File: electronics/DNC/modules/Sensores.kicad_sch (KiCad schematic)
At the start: 10 parts

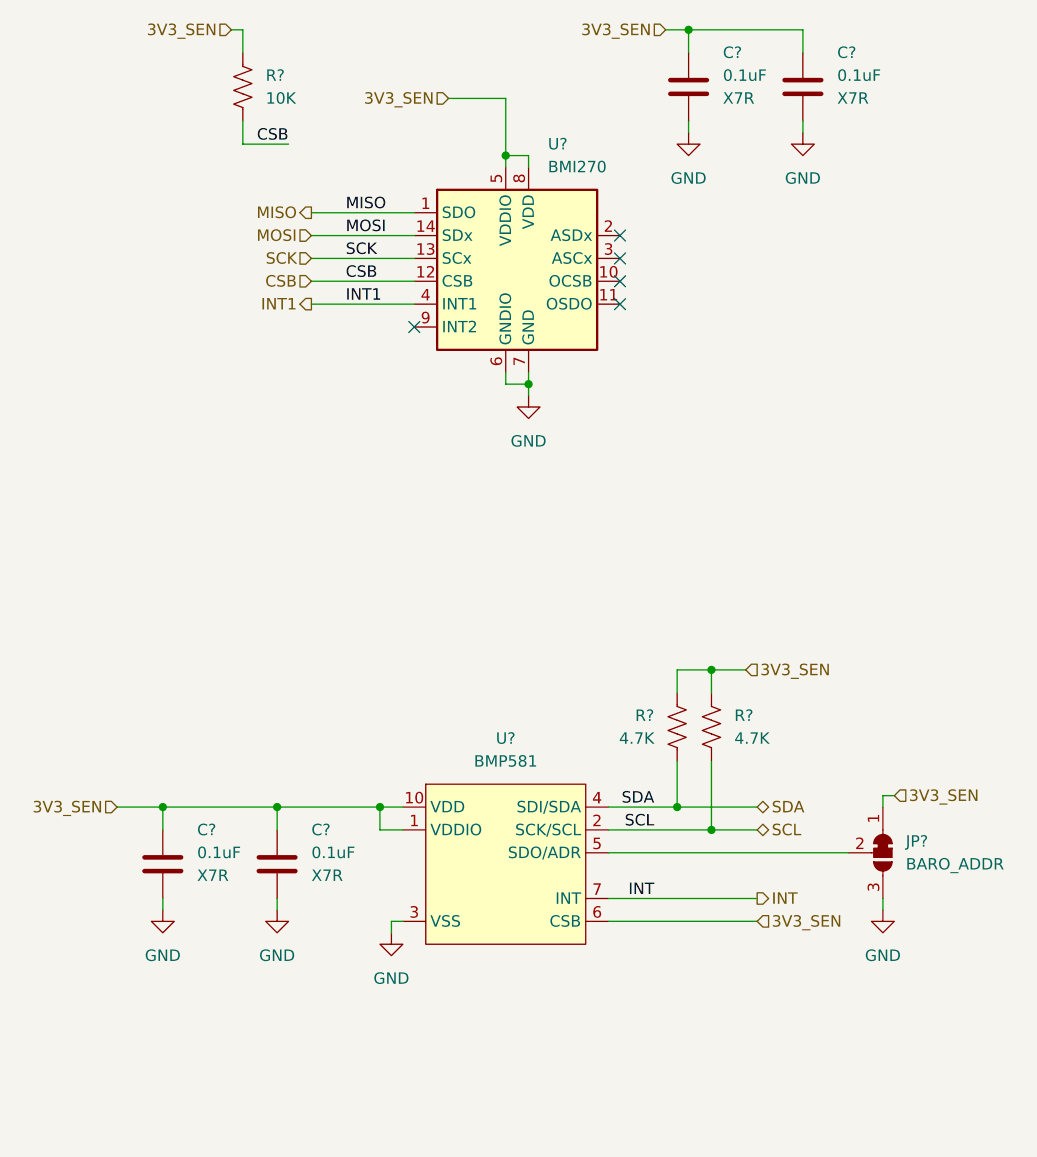
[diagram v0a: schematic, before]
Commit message: Se enlazó el BMP581 a SJ_Sensor y la hoja de dibujo a sj_library
- Sensores: BMP581 pasa de MSS_Sensor (librería de MS4M) a SJ_Sensor:BMP581 con la
  huella Bosch_LGA-10_2x2mm_P0.5mm (antes usaba la huella del LPS22). Reruteado;
  netlist verificado: mismas redes, y VSS 8/9 ahora conectados explícitamente a GND.
- DNC.kicad_pro: hoja de dibujo desde ${SJ_KICAD_LIBS}/sj_library/worksheets/SJ_Page.kicad_wks
  (antes ${MS4M_TEMPLATE}).
- El proyecto ya no depende de ninguna librería de MS4M.

Co-Authored-By: Claude Opus 5.5 <noreply@anthropic.com>
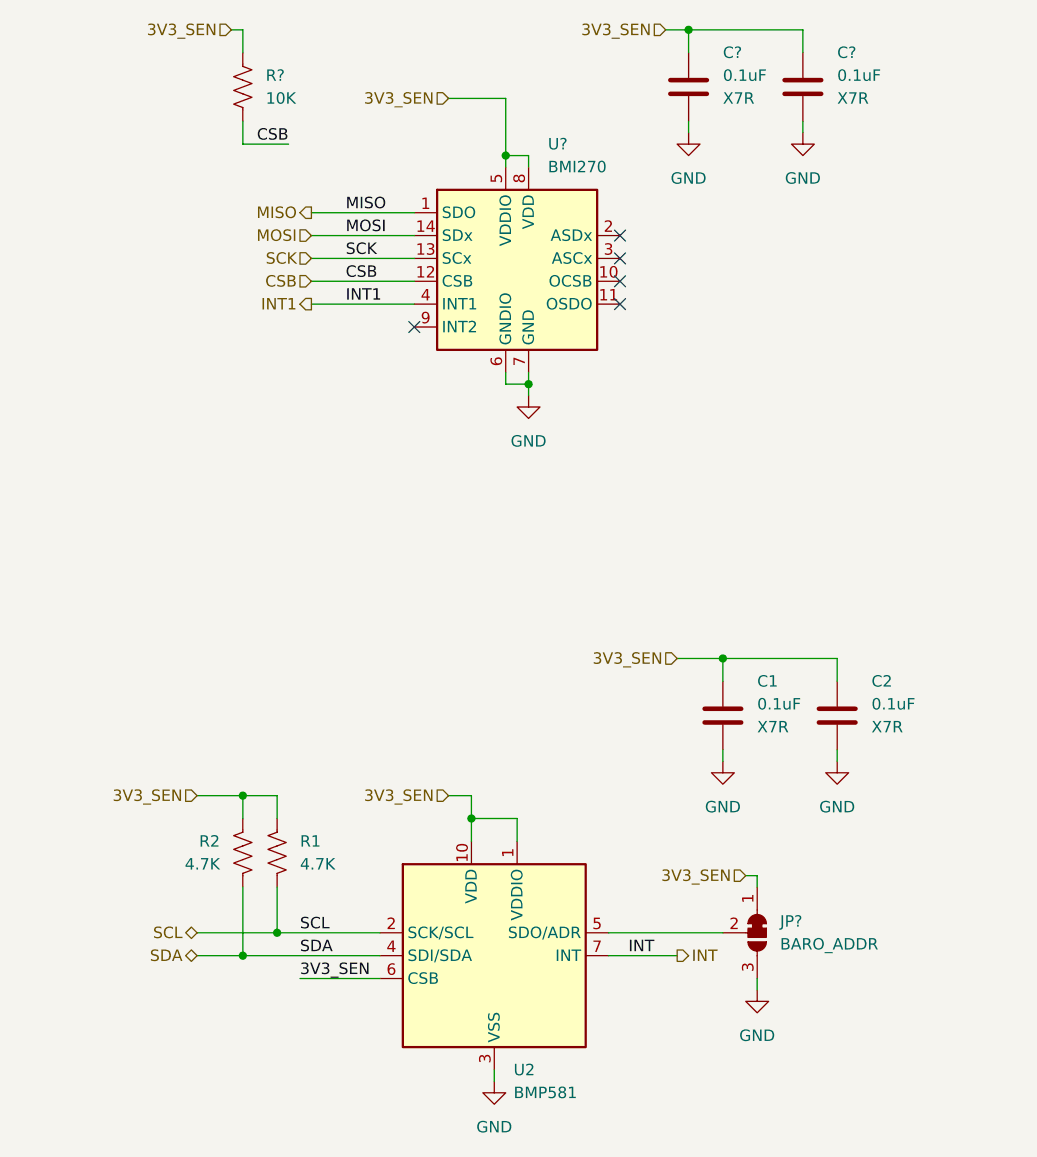
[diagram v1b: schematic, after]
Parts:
- removed C? (x2): 0.1uF, symbol Device:C
- removed R? (x2): 4.7K, symbol Device:R_US
- removed U?: BMP581, Package_LGA:ST_HLGA-10_2x2mm_P0.5mm_LayoutBorder3x2y, symbol MSS_Sensor:BMP581
- added C1, C2: 0.1uF, symbol Device:C
- added R1, R2: 4.7K, symbol Device:R_US
- added U2: BMP581, SJ_Sensor:Bosch_LGA-10_2x2mm_P0.5mm, symbol SJ_Sensor:BMP581
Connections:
- net 3V3_SEN: now also C1.1, C2.1, R1.1, R2.1, U2.1 (VDDIO), U2.10 (VDD), U2.6 (CSB)
- net GND: now also C1.2, C2.2, U2.3 (VSS), U2.8 (VSS), U2.9 (VSS)
- net INT: now also U2.7 (INT)
- net SCL: now also R1.2, U2.2 (SCK/SCL)
- net SDA: now also R2.2, U2.4 (SDI/SDA)
- net at JP?.2 (C): now also U2.5 (SDO/ADR)
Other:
- moved on the sheet: JP?

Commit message: XT60 con huella estándar y BMI270 enlazado a SJ_Sensor
- XT60: Gen_devices:AMASS_XT60-M -> Connector_AMASS:AMASS_XT60-M_1x02_P7.20mm_Vertical
  (misma geometría y polaridad: pin 1 GND, pin 2 VIN_RAW), con los campos SJ.
- Sensores: BMI270 pasa de Sensor_Motion:BMI160 a SJ_Sensor:BMI270 (misma geometría;
  netlist idéntico, sin cambios de cableado). Pines sin usar según Bosch: ASDx/ASCx,
  INT2, OCSB y OSDO sin conectar.

Co-Authored-By: Claude Opus 5.5 <noreply@anthropic.com>
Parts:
- removed U?: BMI270, Package_LGA:Bosch_LGA-14_3x2.5mm_P0.5mm, symbol Sensor_Motion:BMI160
- added U?: BMI270, Package_LGA:Bosch_LGA-14_3x2.5mm_P0.5mm, symbol SJ_Sensor:BMI270
- renumbered C1 to C?, C2 to C?, R2 to R?, R1 to R?, U2 to U?
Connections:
- net 3V3_SEN: now also U?.5 (VDDIO), U?.8 (VDD)
- net CSB: now also U?.12 (CSB)
- net GND: now also U?.6 (GNDIO), U?.7 (GND)
- net INT1: now also U?.4 (INT1)
- net MISO: now also U?.1 (SDO)
- net MOSI: now also U?.14 (SDx)
- net SCK: now also U?.13 (SCx)
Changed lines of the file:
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@@
 	)
 	(symbol
-		(lib_id "Sensor_Motion:BMI160")
+		(lib_id "SJ_Sensor:BMI270")
 		(at 82.55 76.2 0)
 		(unit 1)
@@
 			)
 		)
-		(property "Description" "Accelerometer, Gyroscope, 6 Axis Sensor I2C, SPI Output"
+		(property "Description" "6-axis IMU (accelerometer + gyroscope), SPI/I2C, OIS/AUX interface, 1.71-3.6V, LGA-14 3x2.5mm"
 			(at 82.55 76.2 0)
 			(hide yes)
@@
 		(property "Voltage" ""
 			(at 82.55 76.2 0)
+			(hide yes)
 			(show_name no)
 			(do_not_autoplace no)
@@
 		(property "Current" ""
 			(at 82.55 76.2 0)
+			(hide yes)
 			(show_name no)
 			(do_not_autoplace no)
@@
 		(property "TC" ""
 			(at 82.55 76.2 0)
+			(hide yes)
 			(show_name no)
 			(do_not_autoplace no)
@@
 		(property "Power" ""
 			(at 82.55 76.2 0)
+			(hide yes)
 			(show_name no)
 			(do_not_autoplace no)
@@
 		(property "Tol" ""
 			(at 82.55 76.2 0)
-			(show_name no)
-			(do_not_autoplace no)
-			(effects
-				(font
-					(size 1.27 1.27)
-				)
-			)
+			(hide yes)
+			(show_name no)
+			(do_not_autoplace no)
+			(effects
+				(font
+					(size 1.27 1.27)
+				)
+			)
+		)
+		(pin "5"
+		)
+		(pin "12"
 		)
 		(pin "4"
 		)
+		(pin "3"
+		)
+		(pin "1"
+		)
+		(pin "7"
+		)
+		(pin "6"
+		)
+		(pin "9"
+		)
 		(pin "11"
 		)
-		(pin "5"
-		)
-		(pin "6"
-		)
-		(pin "1"
+		(pin "2"
+		)
+		(pin "8"
 		)
 		(pin "10"
 		)
-		(pin "8"
-		)
-		(pin "2"
-		)
-		(pin "12"
-		)
-		(pin "3"
-		)
 		(pin "13"
 		)
-		(pin "9"
-		)
 		(pin "14"
-		)
-		(pin "7"
 		)
 		(instances
@@
 		(dnp no)
 		(fields_autoplaced yes)
-		(property "Reference" "R2"
+		(property "Reference" "R?"
 			(at 48.26 140.9699 0)
 			(show_name no)
@@
 			(project "DNC"
 				(path "/abee636e-ad3a-4ba4-b95f-d0cf4a6d3d85/c7e61742-03fb-4f4f-aef3-37e8cfb255c2"
-					(reference "R2")
+					(reference "R?")
 					(unit 1)
 				)
@@
 		(dnp no)
 		(fields_autoplaced yes)
-		(property "Reference" "C1"
+		(property "Reference" "C?"
 			(at 107.95 123.1899 0)
 			(show_name no)
@@
 			(project "DNC"
 				(path "/abee636e-ad3a-4ba4-b95f-d0cf4a6d3d85/c7e61742-03fb-4f4f-aef3-37e8cfb255c2"
-					(reference "C1")
+					(reference "C?")
 					(unit 1)
 				)
@@
 		(dnp no)
 		(fields_autoplaced yes)
-		(property "Reference" "R1"
+		(property "Reference" "R?"
 			(at 57.15 140.9699 0)
 			(show_name no)
@@
 			(project "DNC"
 				(path "/abee636e-ad3a-4ba4-b95f-d0cf4a6d3d85/c7e61742-03fb-4f4f-aef3-37e8cfb255c2"
-					(reference "R1")
+					(reference "R?")
 					(unit 1)
 				)
@@
 		(dnp no)
 		(fields_autoplaced yes)
-		(property "Reference" "#PWR01"
+		(property "Reference" "#PWR?"
 			(at 78.74 173.99 0)
 			(hide yes)
@@
 			(project "DNC"
 				(path "/abee636e-ad3a-4ba4-b95f-d0cf4a6d3d85/c7e61742-03fb-4f4f-aef3-37e8cfb255c2"
-					(reference "#PWR01")
+					(reference "#PWR?")
 					(unit 1)
 				)
@@
 		(dnp no)
 		(fields_autoplaced yes)
-		(property "Reference" "#PWR02"
+		(property "Reference" "#PWR?"
 			(at 104.14 138.43 0)
 			(hide yes)
@@
 			(project "DNC"
 				(path "/abee636e-ad3a-4ba4-b95f-d0cf4a6d3d85/c7e61742-03fb-4f4f-aef3-37e8cfb255c2"
-					(reference "#PWR02")
+					(reference "#PWR?")
 					(unit 1)
 				)
@@
 		(dnp no)
 		(fields_autoplaced yes)
-		(property "Reference" "U2"
+		(property "Reference" "U?"
 			(at 80.8833 166.37 0)
 			(show_name no)
@@
 			(project "DNC"
 				(path "/abee636e-ad3a-4ba4-b95f-d0cf4a6d3d85/c7e61742-03fb-4f4f-aef3-37e8cfb255c2"
-					(reference "U2")
+					(reference "U?")
 					(unit 1)
 				)
@@
 		(dnp no)
 		(fields_autoplaced yes)
-		(property "Reference" "C2"
+		(property "Reference" "C?"
 			(at 120.65 123.1899 0)
 			(show_name no)
@@
 			(project "DNC"
 				(path "/abee636e-ad3a-4ba4-b95f-d0cf4a6d3d85/c7e61742-03fb-4f4f-aef3-37e8cfb255c2"
-					(reference "C2")
+					(reference "C?")
 					(unit 1)
 				)
@@
 		(dnp no)
 		(fields_autoplaced yes)
-		(property "Reference" "#PWR03"
+		(property "Reference" "#PWR?"
 			(at 116.84 138.43 0)
 			(hide yes)
@@
 			(project "DNC"
 				(path "/abee636e-ad3a-4ba4-b95f-d0cf4a6d3d85/c7e61742-03fb-4f4f-aef3-37e8cfb255c2"
-					(reference "#PWR03")
+					(reference "#PWR?")
 					(unit 1)
 				)
